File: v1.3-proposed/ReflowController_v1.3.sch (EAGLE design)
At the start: 52 parts, among them J1 AVR_SPI_PRG_62X3_LOCK

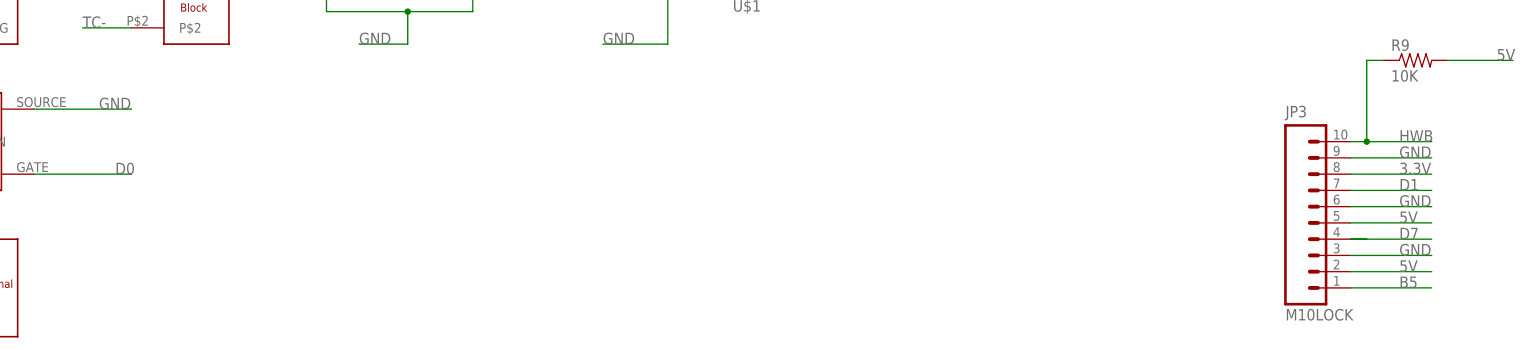
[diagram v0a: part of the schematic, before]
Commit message: Added 2 servo interfaces, many pin swaps
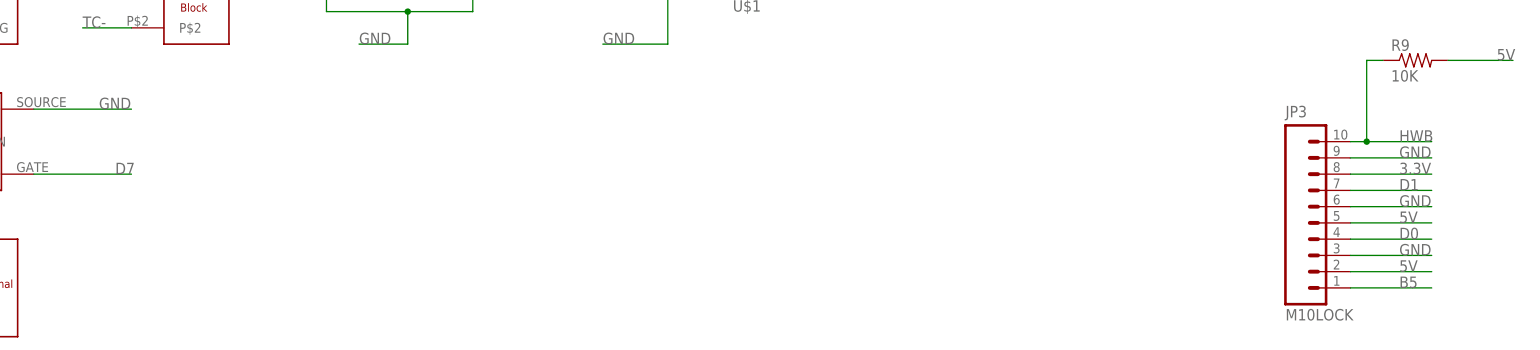
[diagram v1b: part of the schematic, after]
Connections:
- net D0: now also JP3.4; no longer U$16.GATE
- net D7: now also U$16.GATE; no longer JP3.4
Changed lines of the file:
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@@
 </segment>
 <segment>
-<pinref part="JP3" gate="G$1" pin="4"/>
-<wire x1="99.06" y1="-40.64" x2="96.52" y2="-40.64" width="0.1524" layer="91"/>
-<wire x1="96.52" y1="-40.64" x2="109.22" y2="-40.64" width="0.1524" layer="91"/>
-<label x="104.14" y="-40.64" size="1.778" layer="95"/>
+<pinref part="U$16" gate="G$1" pin="GATE"/>
+<wire x1="-109.22" y1="-30.48" x2="-93.98" y2="-30.48" width="0.1524" layer="91"/>
+<label x="-96.52" y="-30.48" size="1.778" layer="95"/>
 </segment>
 </net>
@@
 </segment>
 <segment>
-<pinref part="U$16" gate="G$1" pin="GATE"/>
-<wire x1="-109.22" y1="-30.48" x2="-93.98" y2="-30.48" width="0.1524" layer="91"/>
-<label x="-96.52" y="-30.48" size="1.778" layer="95"/>
-</segment>
-</net>
+<pinref part="JP3" gate="G$1" pin="4"/>
+<wire x1="96.52" y1="-40.64" x2="109.22" y2="-40.64" width="0.1524" layer="91"/>
+<label x="104.14" y="-40.64" size="1.778" layer="95"/>
+</segment>
+</net>

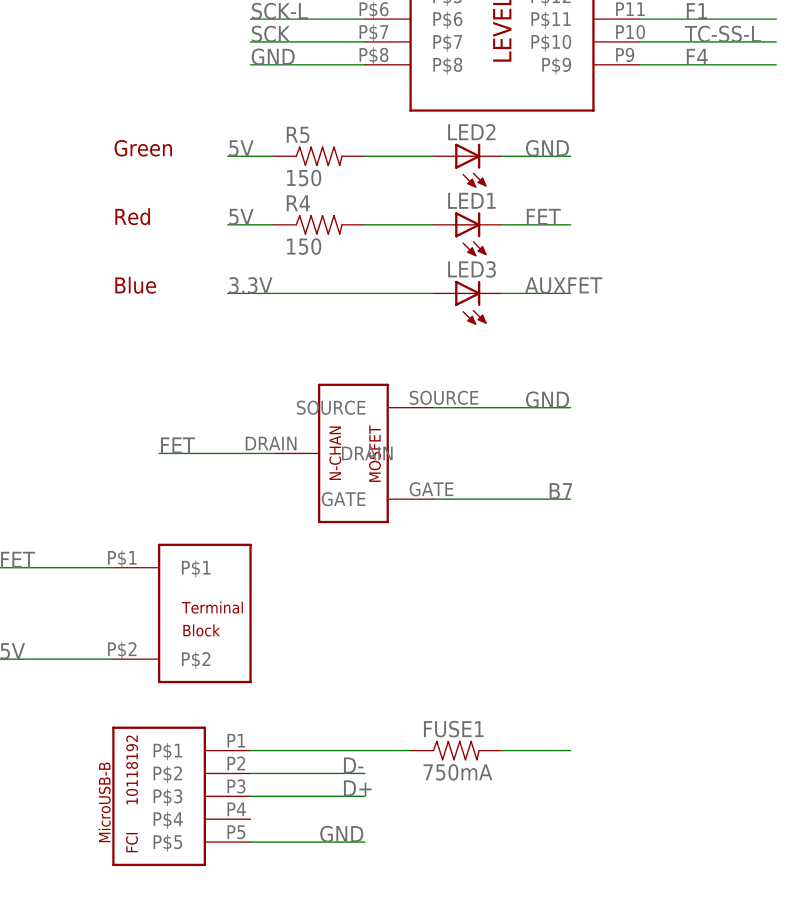
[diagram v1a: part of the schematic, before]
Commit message: Added 2 servo interfaces, many optimizations
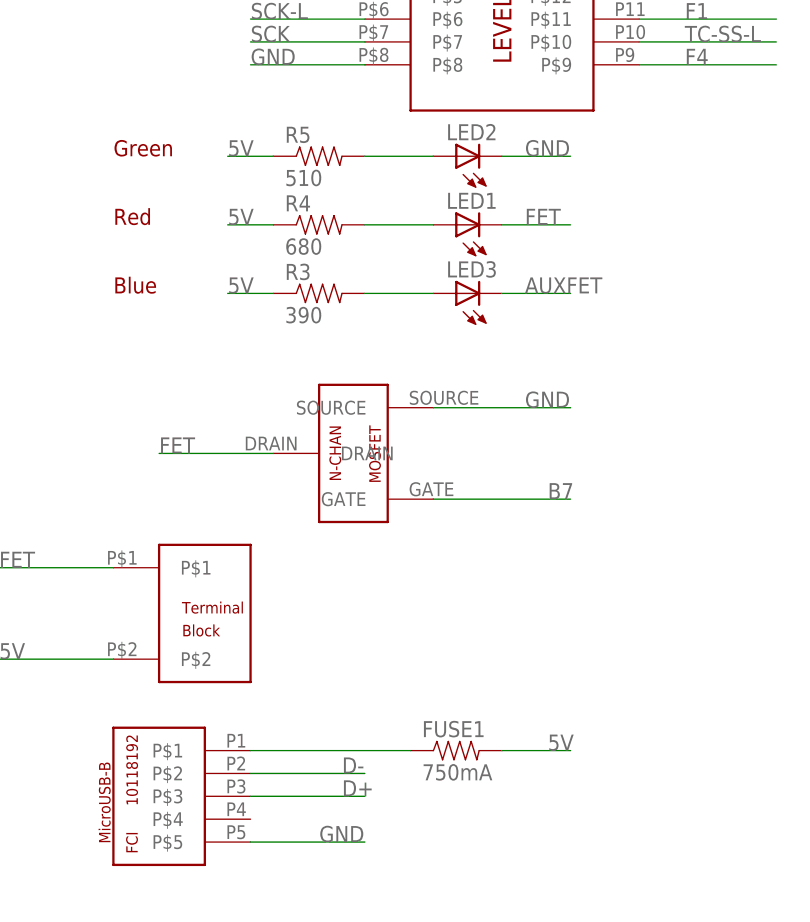
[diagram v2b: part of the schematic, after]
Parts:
- added R3: 390, SparkFun-Passives:RESISTOR0603-RES
- R4: value 150 -> 680
- R5: value 150 -> 510
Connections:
- new net N$6: LED3.A, R3.2
- net 3.3V: no longer LED3.A
- net 5V: now also R3.1
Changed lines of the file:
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@@
 <part name="LED1" library="SparkFun-LED" deviceset="LED" device="0603"/>
 <part name="LED2" library="SparkFun-LED" deviceset="LED" device="0603"/>
-<part name="R4" library="SparkFun-Passives" deviceset="RESISTOR" device="0603-RES" value="150"/>
-<part name="R5" library="SparkFun-Passives" deviceset="RESISTOR" device="0603-RES" value="150"/>
+<part name="R4" library="SparkFun-Passives" deviceset="RESISTOR" device="0603-RES" value="680"/>
+<part name="R5" library="SparkFun-Passives" deviceset="RESISTOR" device="0603-RES" value="510"/>
 <part name="U$13" library="JKCustom" deviceset="CAPTOUCH_ARROW" device=""/>
 <part name="U$14" library="JKCustom" deviceset="CAPTOUCH_ARROW" device=""/>
@@
 <part name="JP3" library="SparkFun-Connectors" deviceset="M10" device="LOCK"/>
 <part name="R9" library="SparkFun-Passives" deviceset="RESISTOR" device="0603-RES" value="10K"/>
+<part name="R3" library="SparkFun-Passives" deviceset="RESISTOR" device="0603-RES" value="390"/>
 </parts>
 <sheets>
@@
 <instance part="JP3" gate="G$1" x="86.36" y="-30.48"/>
 <instance part="R9" gate="G$1" x="106.68" y="-12.7"/>
+<instance part="R3" gate="G$1" x="-109.22" y="109.22"/>
 </instances>
 <busses>
@@
 <pinref part="FUSE1" gate="G$1" pin="2"/>
 <wire x1="-88.9" y1="58.42" x2="-81.28" y2="58.42" width="0.1524" layer="91"/>
+<label x="-83.82" y="58.42" size="1.778" layer="95"/>
 </segment>
 <segment>
@@
 <wire x1="111.76" y1="-12.7" x2="121.92" y2="-12.7" width="0.1524" layer="91"/>
 <label x="119.38" y="-12.7" size="1.778" layer="95"/>
+</segment>
+<segment>
+<pinref part="R3" gate="G$1" pin="1"/>
+<wire x1="-114.3" y1="109.22" x2="-119.38" y2="109.22" width="0.1524" layer="91"/>
+<label x="-119.38" y="109.22" size="1.778" layer="95"/>
 </segment>
 </net>
@@
 <junction x="-99.06" y="10.16"/>
 <wire x1="-99.06" y1="10.16" x2="-111.76" y2="10.16" width="0.1524" layer="91"/>
-</segment>
-<segment>
-<pinref part="LED3" gate="G$1" pin="A"/>
-<wire x1="-96.52" y1="109.22" x2="-119.38" y2="109.22" width="0.1524" layer="91"/>
-<label x="-119.38" y="109.22" size="1.778" layer="95"/>
 </segment>
 <segment>
@@
 </segment>
 </net>
+<net name="N$6" class="0">
+<segment>
+<pinref part="LED3" gate="G$1" pin="A"/>
+<pinref part="R3" gate="G$1" pin="2"/>
+<wire x1="-96.52" y1="109.22" x2="-104.14" y2="109.22" width="0.1524" layer="91"/>
+</segment>
+</net>
